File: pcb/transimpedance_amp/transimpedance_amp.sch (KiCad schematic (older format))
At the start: 34 parts, among them P1 CONN_01X05, P2 CONN_01X05, P3 CONN_01X05, P4 CONN_01X05, P5 CONN_01X05, P6 CONN_01X05, P7 CONN_01X05, P8 CONN_01X05, U1 AD8616

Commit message: Done with layouting so far.
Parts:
- added TP3: TEST, Testpoints:TP_SMD_quadr_3mm, symbol TEST
- D2: value BPW34FA -> BPW34
- TP1, TP2: footprint Wire_Pads:SolderWirePad_single_1mmDrill -> Testpoints:TP_SMD_quadr_3mm
- TP4: renamed from TP3; footprint Wire_Pads:SolderWirePad_single_1mmDrill -> Testpoints:TP_SMD_quadr_3mm
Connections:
- net GND: now also TP3.1
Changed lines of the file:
@@
 F 0 "TP1" H 4600 3500 50  0000 C BNN
 F 1 "TEST" H 4600 3450 50  0000 C CNN
-F 2 "Wire_Pads:SolderWirePad_single_1mmDrill" H 4600 3200 50  0001 C CNN
+F 2 "Testpoints:TP_SMD_quadr_3mm" H 4600 3200 50  0001 C CNN
 F 3 "" H 4600 3200 50  0000 C CNN
 	1    4600 3200
@@
 P 7250 4600
 F 0 "D2" H 7270 4670 50  0000 L CNN
-F 1 "BPW34FA" H 7210 4490 50  0000 C CNN
+F 1 "BPW34" H 7210 4490 50  0000 C CNN
 F 2 "Photodiodes:BPW34FA" H 7200 4600 50  0001 C CNN
 F 3 "http://www.farnell.com/datasheets/2046123.pdf" H 7200 4600 50  0001 C CNN
@@
 $EndComp
 $Comp
-L TEST TP3
+L TEST TP4
 U 1 1 58FE922E
 P 7050 3200
-F 0 "TP3" H 7050 3500 50  0000 C BNN
+F 0 "TP4" H 7050 3500 50  0000 C BNN
 F 1 "TEST" H 7050 3450 50  0000 C CNN
-F 2 "Wire_Pads:SolderWirePad_single_1mmDrill" H 7050 3200 50  0001 C CNN
+F 2 "Testpoints:TP_SMD_quadr_3mm" H 7050 3200 50  0001 C CNN
 F 3 "" H 7050 3200 50  0000 C CNN
 	1    7050 3200
@@
 F 0 "TP2" H 6050 2200 50  0000 C BNN
 F 1 "TEST" H 6050 2150 50  0000 C CNN
-F 2 "Wire_Pads:SolderWirePad_single_1mmDrill" H 6050 1900 50  0001 C CNN
+F 2 "Testpoints:TP_SMD_quadr_3mm" H 6050 1900 50  0001 C CNN
 F 3 "" H 6050 1900 50  0000 C CNN
 	1    6050 1900
@@
 	1    0    0    -1
 $EndComp
+$Comp
+L GND #PWR08
+U 1 1 58FF10F3
+P 6050 2600
+F 0 "#PWR08" H 6050 2350 50  0001 C CNN
+F 1 "GND" H 6050 2450 50  0000 C CNN
+F 2 "" H 6050 2600 50  0000 C CNN
+F 3 "" H 6050 2600 50  0000 C CNN
+	1    6050 2600
+	1    0    0    -1
+$EndComp
+$Comp
+L TEST TP3
+U 1 1 58FF116B
+P 6050 2450
+F 0 "TP3" H 6050 2750 50  0000 C BNN
+F 1 "TEST" H 6050 2700 50  0000 C CNN
+F 2 "Testpoints:TP_SMD_quadr_3mm" H 6050 2450 50  0001 C CNN
+F 3 "" H 6050 2450 50  0000 C CNN
+	1    6050 2450
+	-1   0    0    -1
+$EndComp
+Wire Wire Line
+	6050 2450 6050 2600
 $EndSCHEMATC

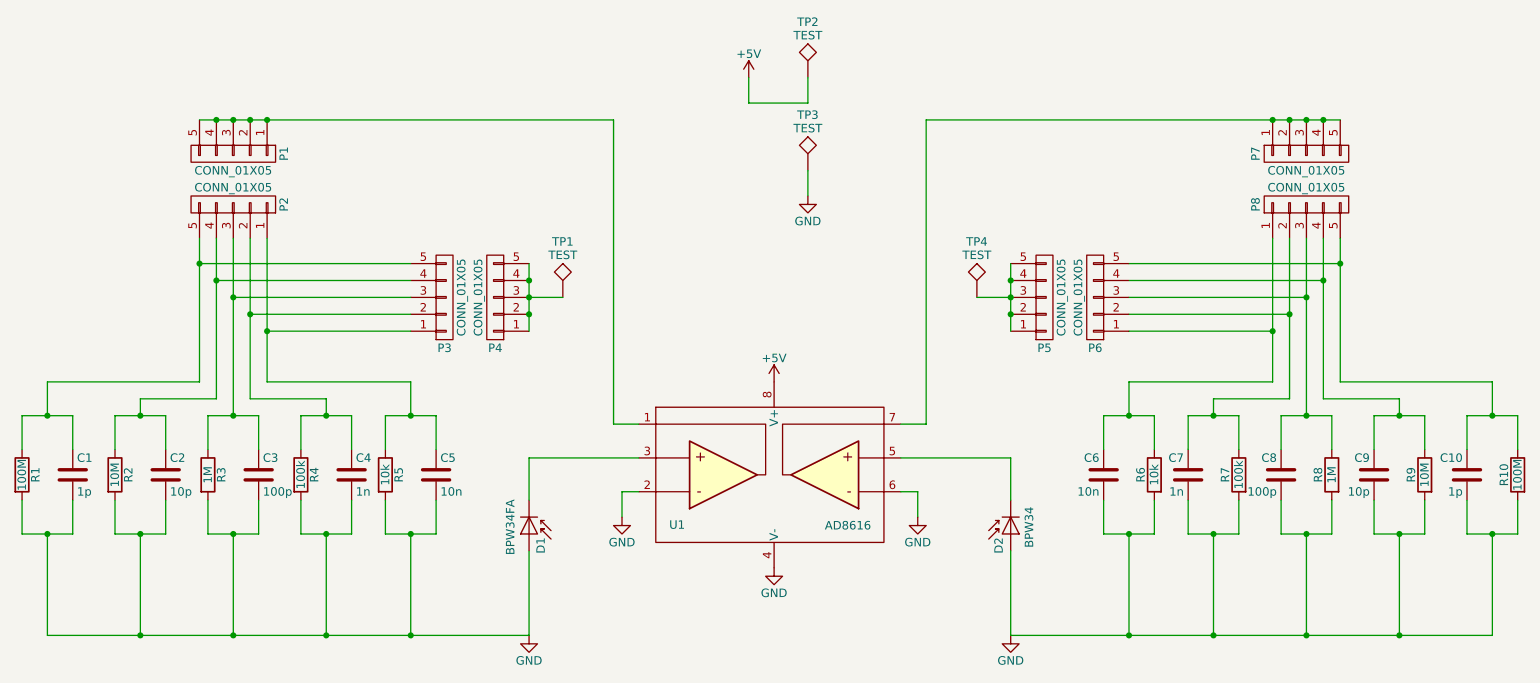
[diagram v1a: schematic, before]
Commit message: Found a design error. Has to be corrected.
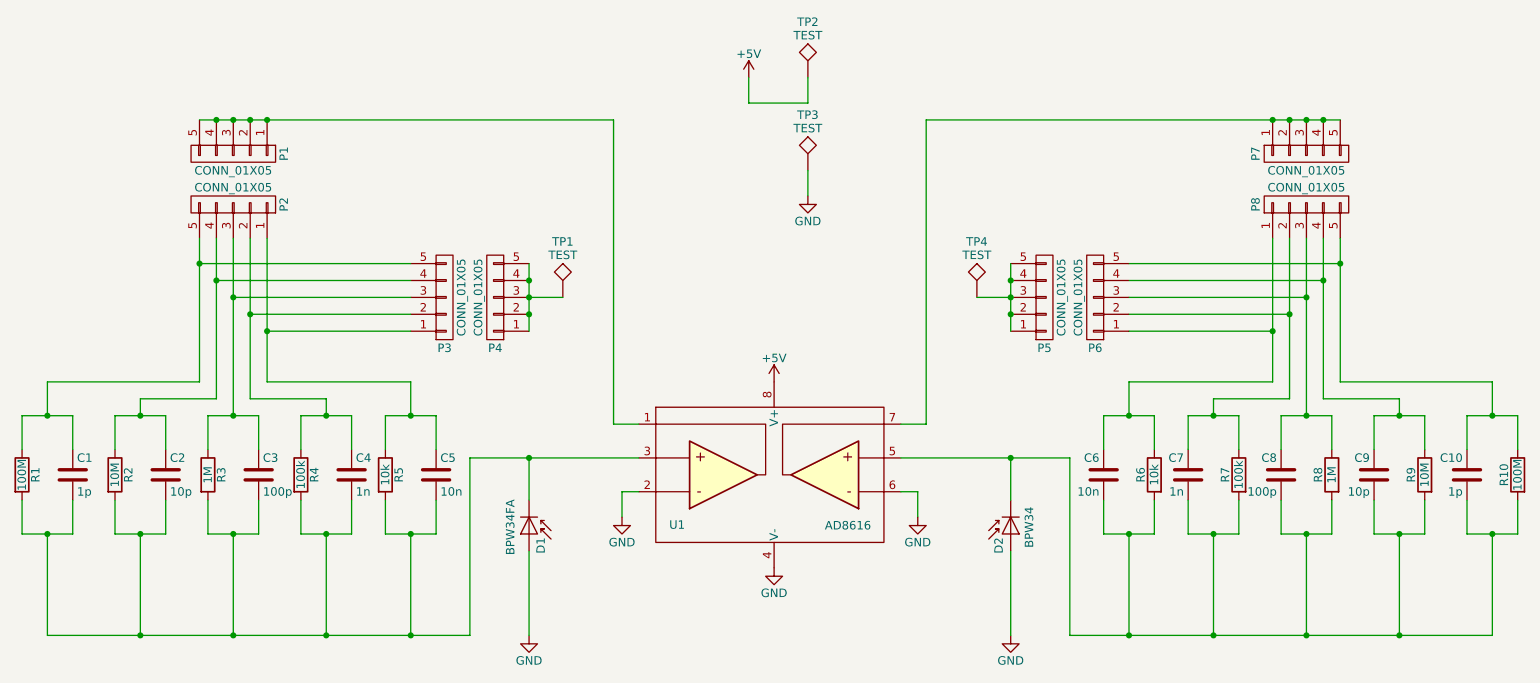
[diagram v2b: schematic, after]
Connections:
- net GND: no longer C1.2, C10.2, C2.2, C3.2, C4.2, C5.2, C6.2, C7.2, C8.2, C9.2, R1.2, R10.2, R2.2, R3.2, R4.2, R5.2, R6.2, R7.2, R8.2, R9.2
- net at D1.1 (K), U1.3: now also C1.2, C2.2, C3.2, C4.2, C5.2, R1.2, R2.2, R3.2, R4.2, R5.2
- net at D2.1 (K), U1.5: now also C10.2, C6.2, C7.2, C8.2, C9.2, R10.2, R6.2, R7.2, R8.2, R9.2
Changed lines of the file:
@@
 	4950 4350 4950 4500
 Wire Wire Line
-	5050 4150 4400 4150
+	4050 4150 5050 4150
 Wire Wire Line
 	4400 5200 4400 4700
@@
 Wire Wire Line
 	4400 3200 4600 3200
-Wire Wire Line
-	1550 5200 4400 5200
 Wire Wire Line
 	1950 4100 1950 3900
@@
 Connection ~ 2100 5200
 Wire Wire Line
-	2650 4600 2650 5200
+	2650 5200 2650 4600
 Connection ~ 2650 5200
 Wire Wire Line
-	3200 4600 3200 5200
+	3200 5200 3200 4600
 Connection ~ 3200 5200
 Wire Wire Line
-	3700 4600 3700 5200
+	3700 5200 3700 4600
 Connection ~ 3700 5200
 $Comp
@@
 	8800 2850 8800 3700
 Wire Wire Line
-	6600 4150 7250 4150
+	6600 4150 7600 4150
 Wire Wire Line
 	7250 5200 7250 4700
@@
 Wire Wire Line
 	7250 3200 7050 3200
-Wire Wire Line
-	7250 5200 10100 5200
 Wire Wire Line
 	9700 3900 9700 4100
@@
 	10100 5200 10100 4600
 Wire Wire Line
-	9550 4600 9550 5200
+	9550 5200 9550 4600
 Connection ~ 9550 5200
 Wire Wire Line
-	9000 4600 9000 5200
+	9000 5200 9000 4600
 Connection ~ 9000 5200
 Wire Wire Line
-	8450 4600 8450 5200
+	8450 5200 8450 4600
 Connection ~ 8450 5200
 Wire Wire Line
@@
 Wire Wire Line
 	6050 2450 6050 2600
+Wire Wire Line
+	1550 5200 4050 5200
+Wire Wire Line
+	4050 5200 4050 4150
+Connection ~ 4400 4150
+Wire Wire Line
+	7600 5200 10100 5200
+Wire Wire Line
+	7600 4150 7600 5200
+Connection ~ 7250 4150
 $EndSCHEMATC

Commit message: Finished layout. Sill room for optimization.
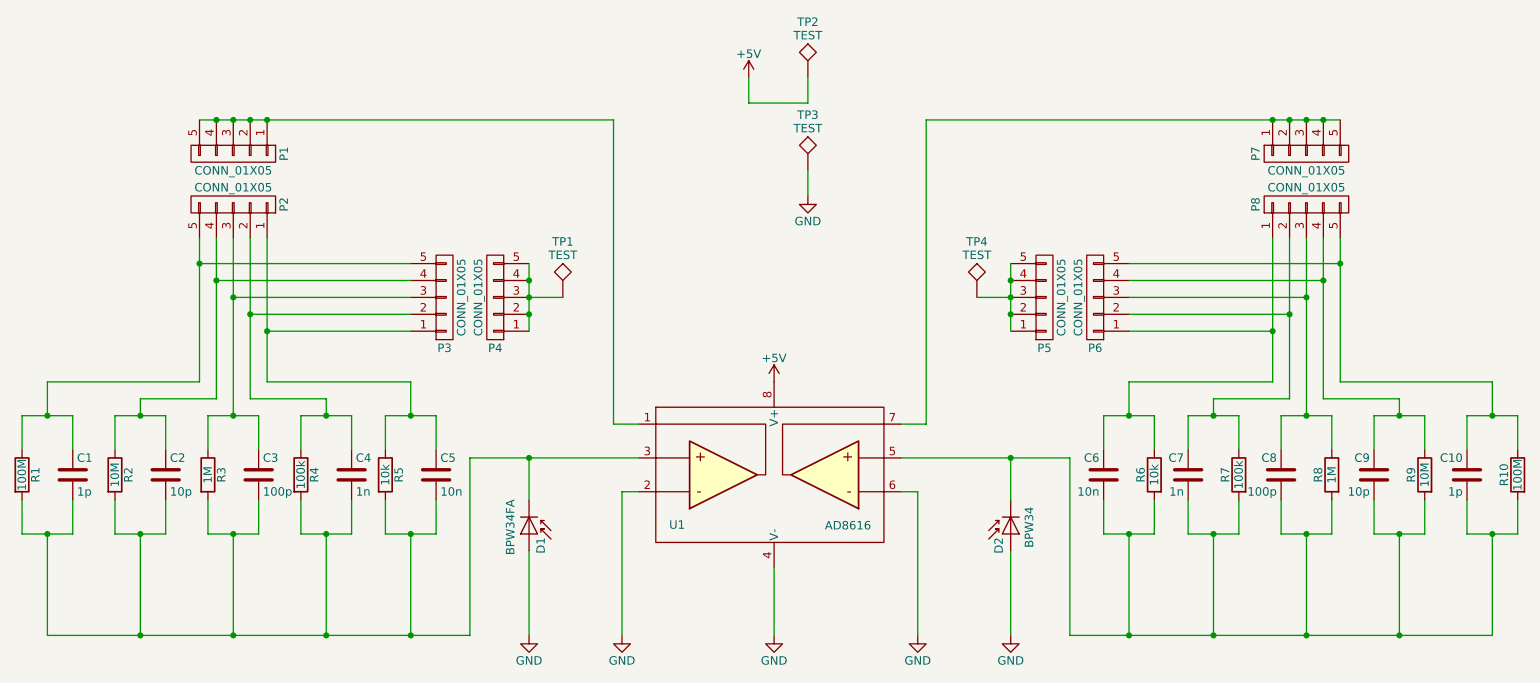
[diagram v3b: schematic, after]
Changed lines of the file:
@@
 L GND #PWR01
 U 1 1 58FDDDA3
-P 4950 4500
-F 0 "#PWR01" H 4950 4250 50  0001 C CNN
-F 1 "GND" H 4950 4350 50  0000 C CNN
-F 2 "" H 4950 4500 50  0000 C CNN
-F 3 "" H 4950 4500 50  0000 C CNN
-	1    4950 4500
+P 4950 5200
+F 0 "#PWR01" H 4950 4950 50  0001 C CNN
+F 1 "GND" H 4950 5050 50  0000 C CNN
+F 2 "" H 4950 5200 50  0000 C CNN
+F 3 "" H 4950 5200 50  0000 C CNN
+	1    4950 5200
 	1    0    0    -1
 $EndComp
@@
 L GND #PWR03
 U 1 1 58FDE652
-P 5850 4800
-F 0 "#PWR03" H 5850 4550 50  0001 C CNN
-F 1 "GND" H 5850 4650 50  0000 C CNN
-F 2 "" H 5850 4800 50  0000 C CNN
-F 3 "" H 5850 4800 50  0000 C CNN
-	1    5850 4800
+P 5850 5200
+F 0 "#PWR03" H 5850 4950 50  0001 C CNN
+F 1 "GND" H 5850 5050 50  0000 C CNN
+F 2 "" H 5850 5200 50  0000 C CNN
+F 3 "" H 5850 5200 50  0000 C CNN
+	1    5850 5200
 	1    0    0    -1
 $EndComp
@@
 	1400 4400 1400 4600
 Wire Wire Line
-	1400 4600 1700 4600
+	1400 4600 1550 4600
+Wire Wire Line
+	1550 4600 1700 4600
 Wire Wire Line
 	1700 4600 1700 4400
@@
 	1700 3900 1700 4100
 Wire Wire Line
-	1400 3900 1700 3900
+	1400 3900 1550 3900
+Wire Wire Line
+	1550 3900 1700 3900
 Wire Wire Line
 	1400 3900 1400 4100
 Wire Wire Line
-	1950 4600 2250 4600
+	1950 4600 2100 4600
+Wire Wire Line
+	2100 4600 2250 4600
 Wire Wire Line
 	2250 4600 2250 4400
@@
 	2250 3900 2250 4100
 Wire Wire Line
-	1950 3900 2250 3900
+	1950 3900 2100 3900
+Wire Wire Line
+	2100 3900 2250 3900
 Wire Wire Line
 	2500 4400 2500 4600
 Wire Wire Line
-	2500 4600 2800 4600
+	2500 4600 2650 4600
+Wire Wire Line
+	2650 4600 2800 4600
 Wire Wire Line
 	2800 4600 2800 4400
@@
 	2800 3900 2800 4100
 Wire Wire Line
-	2500 3900 2800 3900
+	2500 3900 2650 3900
+Wire Wire Line
+	2650 3900 2800 3900
 Wire Wire Line
 	2500 3900 2500 4100
@@
 	3050 4400 3050 4600
 Wire Wire Line
-	3050 4600 3350 4600
+	3050 4600 3200 4600
+Wire Wire Line
+	3200 4600 3350 4600
 Wire Wire Line
 	3350 4600 3350 4400
@@
 	3350 3900 3350 4100
 Wire Wire Line
-	3050 3900 3350 3900
+	3050 3900 3200 3900
+Wire Wire Line
+	3200 3900 3350 3900
 Wire Wire Line
 	3050 3900 3050 4100
@@
 	3550 4400 3550 4600
 Wire Wire Line
-	3550 4600 3850 4600
+	3550 4600 3700 4600
+Wire Wire Line
+	3700 4600 3850 4600
 Wire Wire Line
 	3850 4600 3850 4400
@@
 	3850 3900 3850 4100
 Wire Wire Line
-	3550 3900 3850 3900
+	3550 3900 3700 3900
+Wire Wire Line
+	3700 3900 3850 3900
 Wire Wire Line
 	3550 3900 3550 4100
 Wire Wire Line
-	2650 2850 2650 3900
+	2650 2850 2650 3200
+Wire Wire Line
+	2650 3200 2650 3900
 Connection ~ 2650 3900
 Wire Wire Line
@@
 	2100 3800 2550 3800
 Wire Wire Line
-	2550 3800 2550 2850
+	2550 3800 2550 3100
+Wire Wire Line
+	2550 3100 2550 2850
 Connection ~ 2100 3900
 Wire Wire Line
-	2450 2850 2450 3700
+	2450 2850 2450 3000
+Wire Wire Line
+	2450 3000 2450 3700
 Wire Wire Line
 	2450 3700 1550 3700
 Wire Wire Line
-	2750 2850 2750 3800
-Wire Wire Line
-	2850 2850 2850 3700
+	2750 2850 2750 3300
+Wire Wire Line
+	2750 3300 2750 3800
+Wire Wire Line
+	2850 2850 2850 3400
+Wire Wire Line
+	2850 3400 2850 3700
 Wire Wire Line
 	5050 4350 4950 4350
 Wire Wire Line
-	4950 4350 4950 4500
-Wire Wire Line
-	4050 4150 5050 4150
+	4950 4350 4950 5200
+Wire Wire Line
+	4050 4150 4400 4150
+Wire Wire Line
+	4400 4150 5050 4150
 Wire Wire Line
 	4400 5200 4400 4700
 Wire Wire Line
-	4400 3000 4400 3400
+	4400 3000 4400 3100
+Wire Wire Line
+	4400 3100 4400 3200
+Wire Wire Line
+	4400 3200 4400 3300
+Wire Wire Line
+	4400 3300 4400 3400
 Connection ~ 4400 3100
 Connection ~ 4400 3200
@@
 	3700 3700 3700 3900
 Wire Wire Line
-	2450 2150 4900 2150
+	2450 2150 2550 2150
+Wire Wire Line
+	2550 2150 2650 2150
+Wire Wire Line
+	2650 2150 2750 2150
+Wire Wire Line
+	2750 2150 2850 2150
+Wire Wire Line
+	2850 2150 4900 2150
 Wire Wire Line
 	4900 2150 4900 3950
@@
 L GND #PWR05
 U 1 1 58FE9222
-P 6700 4500
-F 0 "#PWR05" H 6700 4250 50  0001 C CNN
-F 1 "GND" H 6700 4350 50  0000 C CNN
-F 2 "" H 6700 4500 50  0000 C CNN
-F 3 "" H 6700 4500 50  0000 C CNN
-	1    6700 4500
+P 6700 5200
+F 0 "#PWR05" H 6700 4950 50  0001 C CNN
+F 1 "GND" H 6700 5050 50  0000 C CNN
+F 2 "" H 6700 5200 50  0000 C CNN
+F 3 "" H 6700 5200 50  0000 C CNN
+	1    6700 5200
 	-1   0    0    -1
 $EndComp
@@
 	10250 4600 10250 4400
 Wire Wire Line
-	9950 4600 10250 4600
+	9950 4600 10100 4600
+Wire Wire Line
+	10100 4600 10250 4600
 Wire Wire Line
 	9950 4600 9950 4400
@@
 	9950 3900 9950 4100
 Wire Wire Line
-	9950 3900 10250 3900
+	9950 3900 10100 3900
+Wire Wire Line
+	10100 3900 10250 3900
 Wire Wire Line
 	10250 3900 10250 4100
 Wire Wire Line
-	9400 4600 9700 4600
+	9400 4600 9550 4600
+Wire Wire Line
+	9550 4600 9700 4600
 Wire Wire Line
 	9400 4600 9400 4400
@@
 	9400 3900 9400 4100
 Wire Wire Line
-	9400 3900 9700 3900
+	9400 3900 9550 3900
+Wire Wire Line
+	9550 3900 9700 3900
 Wire Wire Line
 	9150 4600 9150 4400
 Wire Wire Line
-	8850 4600 9150 4600
+	8850 4600 9000 4600
+Wire Wire Line
+	9000 4600 9150 4600
 Wire Wire Line
 	8850 4600 8850 4400
@@
 	8850 3900 8850 4100
 Wire Wire Line
-	8850 3900 9150 3900
+	8850 3900 9000 3900
+Wire Wire Line
+	9000 3900 9150 3900
 Wire Wire Line
 	9150 3900 9150 4100
@@
 	8600 4600 8600 4400
 Wire Wire Line
-	8300 4600 8600 4600
+	8300 4600 8450 4600
+Wire Wire Line
+	8450 4600 8600 4600
 Wire Wire Line
 	8300 4600 8300 4400
@@
 	8300 3900 8300 4100
 Wire Wire Line
-	8300 3900 8600 3900
+	8300 3900 8450 3900
+Wire Wire Line
+	8450 3900 8600 3900
 Wire Wire Line
 	8600 3900 8600 4100
@@
 	8100 4600 8100 4400
 Wire Wire Line
-	7800 4600 8100 4600
+	7800 4600 7950 4600
+Wire Wire Line
+	7950 4600 8100 4600
 Wire Wire Line
 	7800 4600 7800 4400
@@
 	7800 3900 7800 4100
 Wire Wire Line
-	7800 3900 8100 3900
+	7800 3900 7950 3900
+Wire Wire Line
+	7950 3900 8100 3900
 Wire Wire Line
 	8100 3900 8100 4100
 Wire Wire Line
-	9000 2850 9000 3900
+	9000 2850 9000 3200
+Wire Wire Line
+	9000 3200 9000 3900
 Connection ~ 9000 3900
 Wire Wire Line
@@
 	9550 3800 9100 3800
 Wire Wire Line
-	9100 3800 9100 2850
+	9100 3800 9100 3100
+Wire Wire Line
+	9100 3100 9100 2850
 Connection ~ 9550 3900
 Wire Wire Line
-	9200 2850 9200 3700
+	9200 2850 9200 3000
+Wire Wire Line
+	9200 3000 9200 3700
 Wire Wire Line
 	9200 3700 10100 3700
 Wire Wire Line
-	8900 2850 8900 3800
-Wire Wire Line
-	8800 2850 8800 3700
-Wire Wire Line
-	6600 4150 7600 4150
+	8900 2850 8900 3300
+Wire Wire Line
+	8900 3300 8900 3800
+Wire Wire Line
+	8800 2850 8800 3400
+Wire Wire Line
+	8800 3400 8800 3700
+Wire Wire Line
+	6600 4150 7250 4150
+Wire Wire Line
+	7250 4150 7600 4150
 Wire Wire Line
 	7250 5200 7250 4700
 Wire Wire Line
-	7250 3000 7250 3400
+	7250 3000 7250 3100
+Wire Wire Line
+	7250 3100 7250 3200
+Wire Wire Line
+	7250 3200 7250 3300
+Wire Wire Line
+	7250 3300 7250 3400
 Connection ~ 7250 3100
 Connection ~ 7250 3200
@@
 	7950 3700 7950 3900
 Wire Wire Line
-	6750 2150 9200 2150
+	6750 2150 8800 2150
+Wire Wire Line
+	8800 2150 8900 2150
+Wire Wire Line
+	8900 2150 9000 2150
+Wire Wire Line
+	9000 2150 9100 2150
+Wire Wire Line
+	9100 2150 9200 2150
 Wire Wire Line
 	6750 2150 6750 3950
@@
 	6600 4350 6700 4350
 Wire Wire Line
-	6700 4350 6700 4500
+	6700 4350 6700 5200
 Wire Wire Line
 	3200 3800 3200 3900
@@
 	6050 2450 6050 2600
 Wire Wire Line
-	1550 5200 4050 5200
+	1550 5200 2100 5200
+Wire Wire Line
+	2100 5200 2650 5200
+Wire Wire Line
+	2650 5200 3200 5200
+Wire Wire Line
+	3200 5200 3700 5200
+Wire Wire Line
+	3700 5200 4050 5200
 Wire Wire Line
 	4050 5200 4050 4150
 Connection ~ 4400 4150
 Wire Wire Line
-	7600 5200 10100 5200
+	7600 5200 7950 5200
+Wire Wire Line
+	7950 5200 8450 5200
+Wire Wire Line
+	8450 5200 9000 5200
+Wire Wire Line
+	9000 5200 9550 5200
+Wire Wire Line
+	9550 5200 10100 5200
 Wire Wire Line
 	7600 4150 7600 5200
 Connection ~ 7250 4150
+Wire Wire Line
+	5850 4800 5850 5200
 $EndSCHEMATC
